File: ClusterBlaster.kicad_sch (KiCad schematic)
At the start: 20 parts, among them J1 OBD2, J2 Cluster Display, SW1 UP, SW2 DOWN, SW3 ENTER, U1 LM339, U2 L7805, U3 ARDUINO_PRO_MINI

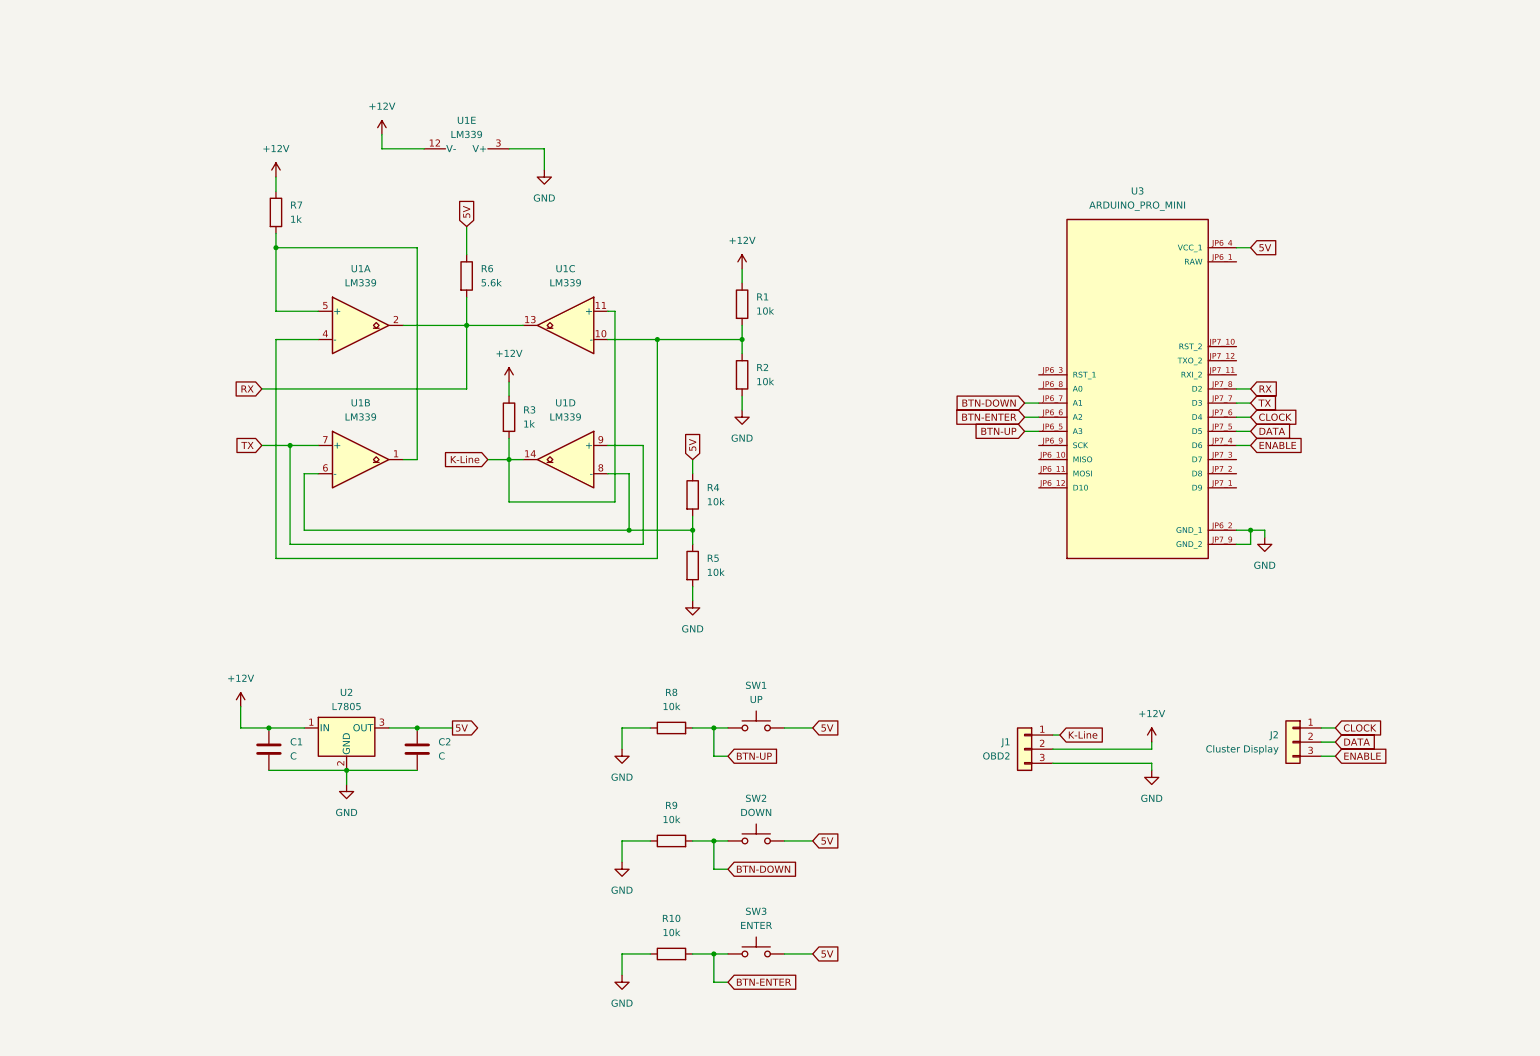
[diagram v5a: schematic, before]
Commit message: Made the schematic cleaner
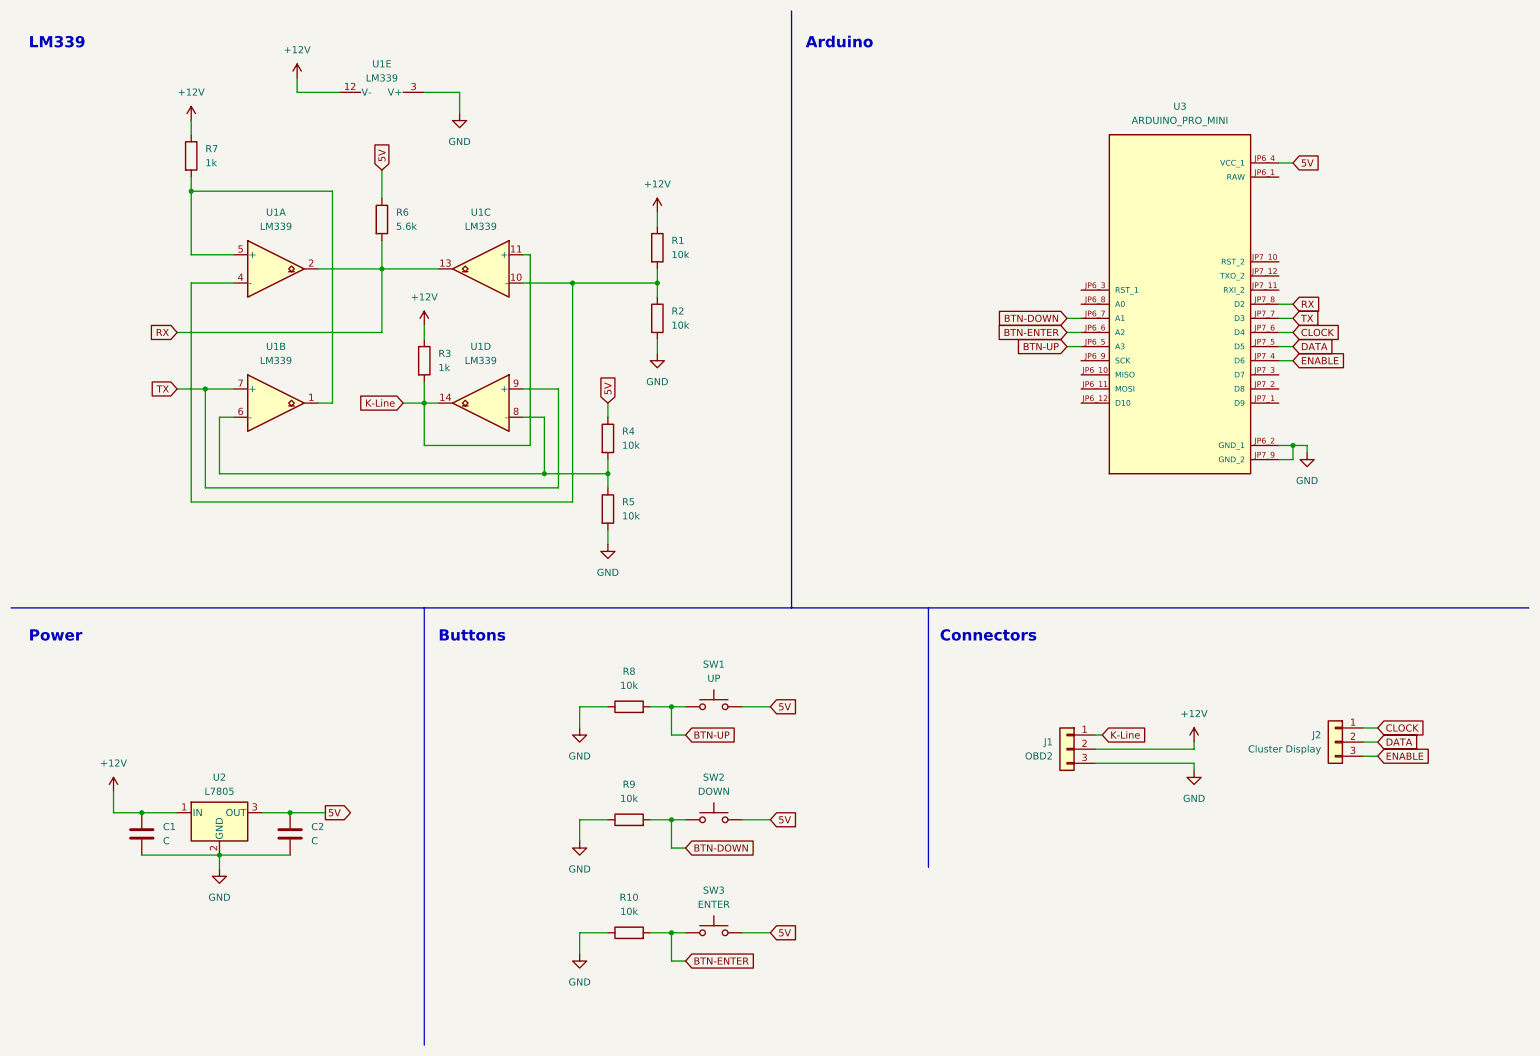
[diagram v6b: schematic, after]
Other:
- note added: "Arduino"
- note added: "Buttons"
- note added: "Connectors"
- note added: "LM339"
- note added: "Power"
- moved on the sheet: C1, C2, J1, J2, R1, R10, R2, R3, R4, R5, R6, R7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
